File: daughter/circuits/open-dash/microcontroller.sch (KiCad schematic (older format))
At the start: 18 parts, among them U10 Temp_Hum_HDC1080DMBR, U9 ESP32-WROOM-32

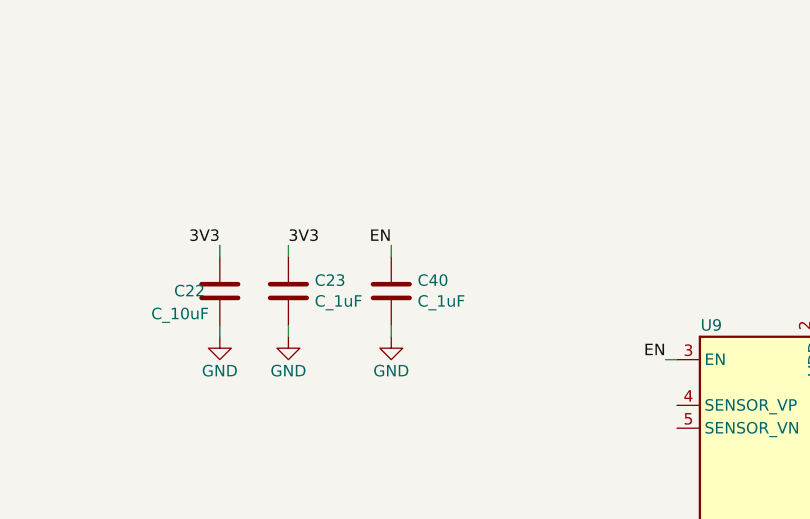
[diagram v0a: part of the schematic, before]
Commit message: send v1.4 to board house. Corrected source-drain on fets.
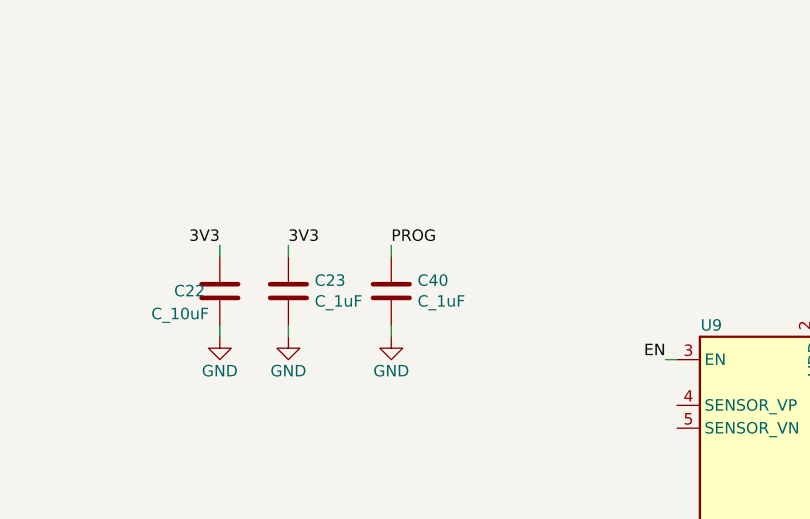
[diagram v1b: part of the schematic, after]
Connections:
- net ESP_EN: no longer C40.1
- net PROG: now also C40.1
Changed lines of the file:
@@
 	1    0    0    -1
 $EndComp
-Text Label 3850 1850 2    50   ~ 0
-EN
+Text Label 3850 1850 0    50   ~ 0
+PROG
 $EndSCHEMATC
